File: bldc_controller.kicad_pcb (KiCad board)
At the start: 4 copper layers, 99.1 x 99.1 mm, 147 parts, among them J1 Conn_01x06_Male, J2 Banana_Jack, J3 Banana_Jack, Q1 2N7002E, Q10 IRLB8721PBF, Q11 IRLB8721PBF, Q2 DMN65D8L-7, Q3 DMN65D8L-7, Q4 MMBT3904, Q5 IRF4905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

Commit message: finished labelling
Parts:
- removed J2, J3: Banana_Jack, Connector_BarrelJack:BarrelJack_CUI_PJ-063AH_Horizontal
- added B1: Banana_Jack, Connector:CalTest_CT3151, F.Cu at (105.4, 47.0)
- added B2: CalTest_CT3151, Connector:CalTest_CT3151, F.Cu at (105.4, 61.0)
- added MH1: MountingHole_Top_Left, MountingHole:MountingHole_2.2mm_M2, F.Cu at (100.5, 38.1)
- added MH2: MountingHole_Top_Right, MountingHole:MountingHole_2.2mm_M2, F.Cu at (198.0, 38.0)
- added MH3: MountingHole_Bottom_Right, MountingHole:MountingHole_2.2mm_M2, F.Cu at (198.0, 138.5)
- added MH4: MountingHole_Bottom_Left, MountingHole:MountingHole_2.2mm_M2, F.Cu at (100.3, 138.5)
- renumbered PhaseC to PhaseA
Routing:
- net PhaseC: track 92.9 -> 106.8 mm, vias 0 -> 1
- net PhaseB: track 139.6 -> 149.8 mm
- net PhaseA: track 190.0 -> 195.5 mm
- net +BATT: track 11.9 -> 16.8 mm
- net Vdrive: track 57.9 -> 61.8 mm
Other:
- board size 99.1 x 99.1 mm -> 102.9 x 105.4 mm
- board text added: "BATT+"
- board text added: "BEMF_A"
- board text added: "BEMF_B"
- board text added: "BEMF_C"
- board text added: "Drivers"
- board text added: "EFUSE_EN"
- board text added: "I_RAW"
- board text added: "Input Connections"
- board text added: "Latching"
- board text added: "Microcontroller"
- board text added: "Neutral"
- board text added: "Overcurrent Threshold"
- board text added: "PhaseA High"
- board text added: "PhaseB High"
- board text added: "PhaseC High"
- board text added: "Power Filters"
- board text added: "Q5 Gate"
- board text added: "V Drive"
- board text added: "nI_Error"

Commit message: fixed small bug
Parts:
- moved B2 1.27 mm to (105.4, 62.2)
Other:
- board text added: "Back EMF"
- board text added: "Output to Motor"
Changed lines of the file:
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@@
   (general
     (thickness 1.6)
-    (drawings 50)
+    (drawings 54)
     (tracks 635)
     (zones 0)
@@
   (page A4)
   (layers
-    (0 F.Cu signal hide)
-    (1 In1.Cu power hide)
-    (2 In2.Cu power hide)
-    (31 B.Cu signal hide)
-    (32 B.Adhes user hide)
-    (33 F.Adhes user hide)
-    (34 B.Paste user hide)
-    (35 F.Paste user hide)
-    (36 B.SilkS user hide)
+    (0 F.Cu signal)
+    (1 In1.Cu power)
+    (2 In2.Cu power)
+    (31 B.Cu signal)
+    (32 B.Adhes user)
+    (33 F.Adhes user)
+    (34 B.Paste user)
+    (35 F.Paste user)
+    (36 B.SilkS user)
     (37 F.SilkS user)
-    (38 B.Mask user hide)
-    (39 F.Mask user hide)
-    (40 Dwgs.User user hide)
-    (41 Cmts.User user hide)
+    (38 B.Mask user)
+    (39 F.Mask user)
+    (40 Dwgs.User user)
+    (41 Cmts.User user)
     (42 Eco1.User user hide)
     (43 Eco2.User user)
     (44 Edge.Cuts user)
     (45 Margin user hide)
-    (46 B.CrtYd user hide)
-    (47 F.CrtYd user hide)
-    (48 B.Fab user hide)
-    (49 F.Fab user hide)
+    (46 B.CrtYd user)
+    (47 F.CrtYd user)
+    (48 B.Fab user)
+    (49 F.Fab user)
   )
   (setup
-    (last_trace_width 0.508)
+    (last_trace_width 0.25)
     (user_trace_width 0.254)
     (user_trace_width 0.508)
@@
     (pad_to_mask_clearance 0)
     (aux_axis_origin 0 0)
-    (visible_elements 7FFFF7FF)
+    (visible_elements 7EE6A077)
     (pcbplotparams
       (layerselection 0x010fc_ffffffff)
@@
   )
   (module Connector:CalTest_CT3151 (layer F.Cu)
-    (at 105.41 60.96)
+    (at 105.41 62.23)
     (descr "Right-angle standard banana jack, http://www.caltestelectronics.com/images/attachments/P315100rH_drawing.pdf")
     (tags "banana jack horizontal")
@@
     )
   )
+  (gr_text "Back EMF" (at 185.42 115.57) (layer F.SilkS)
+    (effects (font (size 1 1) (thickness 0.15)))
+  )
+  (gr_text "Output to Motor" (at 191.77 102.87) (layer F.SilkS)
+    (effects (font (size 1 1) (thickness 0.15)))
+  )
+  (gr_text "Output to Motor" (at 191.77 78.74) (layer F.SilkS)
+    (effects (font (size 1 1) (thickness 0.15)))
+  )
+  (gr_text "Output to Motor" (at 191.77 57.15) (layer F.SilkS)
+    (effects (font (size 1 1) (thickness 0.15)))
+  )
   (gr_text "Q5 Gate" (at 165.1 57.15) (layer F.SilkS)
     (effects (font (size 1 1) (thickness 0.15)))
@@
     (connect_pads (clearance 0.508))
     (min_thickness 0.254)
-    (fill (arc_segments 32) (thermal_gap 0.508) (thermal_bridge_width 0.508))
+    (fill yes (arc_segments 32) (thermal_gap 0.508) (thermal_bridge_width 0.508))
     (polygon
       (pts
@@
     (connect_pads (clearance 0.508))
     (min_thickness 0.254)
-    (fill (arc_segments 32) (thermal_gap 0.508) (thermal_bridge_width 0.508))
+    (fill yes (arc_segments 32) (thermal_gap 0.508) (thermal_bridge_width 0.508))
     (polygon
       (pts

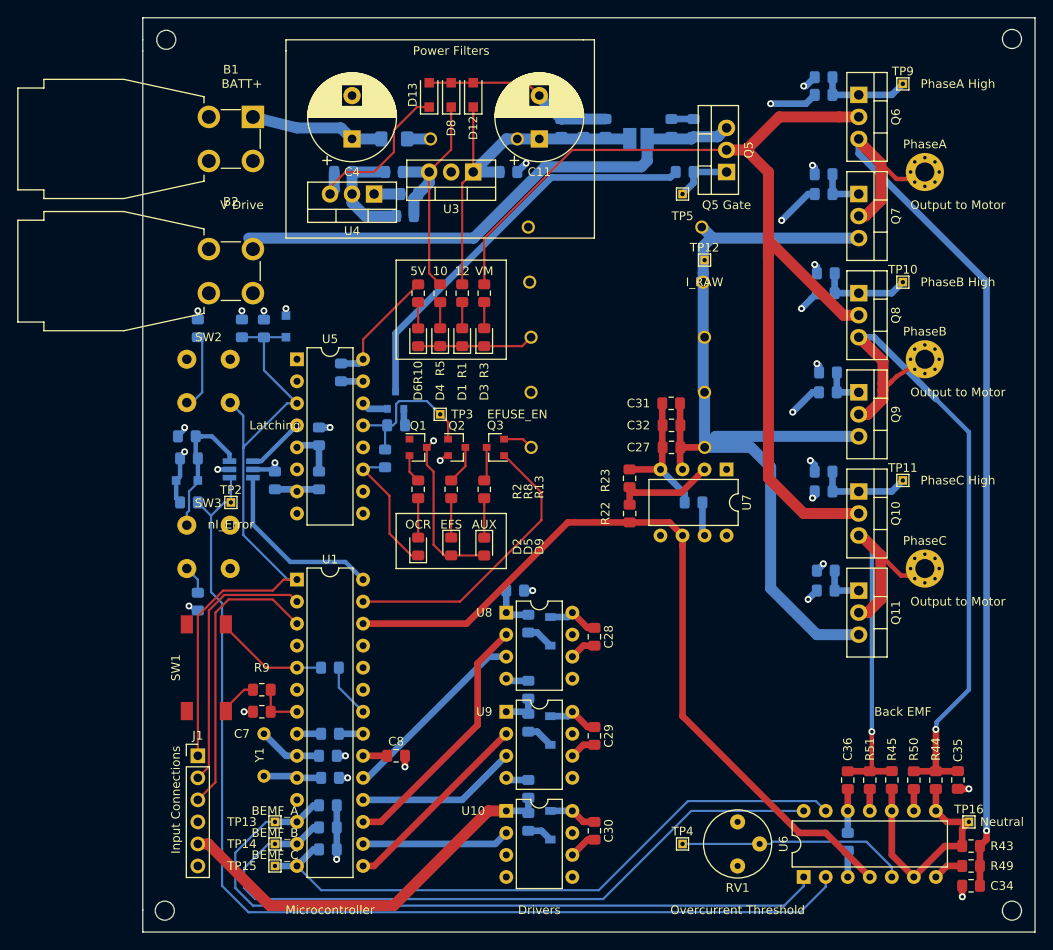
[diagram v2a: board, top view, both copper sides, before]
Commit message: fixed wire thickness
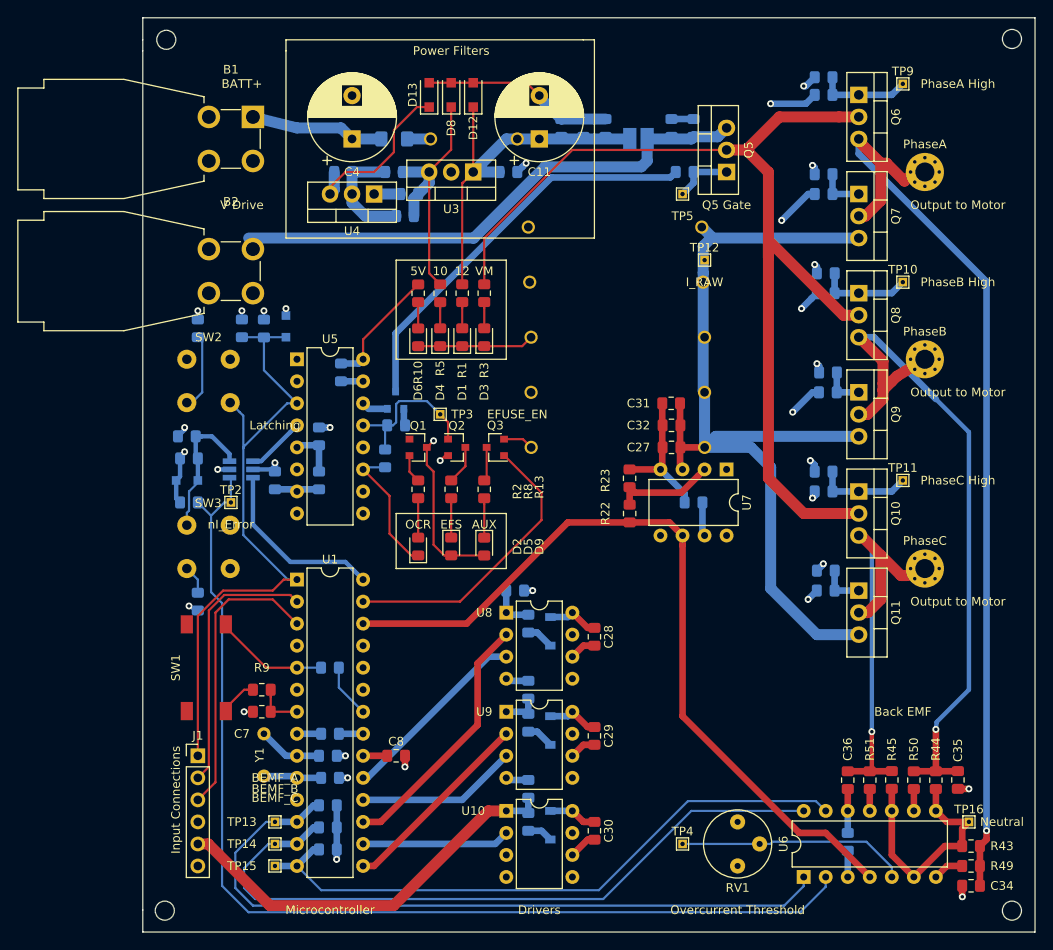
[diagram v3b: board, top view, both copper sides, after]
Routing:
- net PhaseA: track 195.5 -> 198.4 mm
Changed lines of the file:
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@@
     (thickness 1.6)
     (drawings 54)
-    (tracks 635)
+    (tracks 636)
     (zones 0)
     (modules 151)
@@
   (layers
     (0 F.Cu signal)
-    (1 In1.Cu power)
-    (2 In2.Cu power)
-    (31 B.Cu signal)
-    (32 B.Adhes user)
+    (1 In1.Cu power hide)
+    (2 In2.Cu power hide)
+    (31 B.Cu signal hide)
+    (32 B.Adhes user hide)
     (33 F.Adhes user)
-    (34 B.Paste user)
+    (34 B.Paste user hide)
     (35 F.Paste user)
-    (36 B.SilkS user)
+    (36 B.SilkS user hide)
     (37 F.SilkS user)
-    (38 B.Mask user)
+    (38 B.Mask user hide)
     (39 F.Mask user)
     (40 Dwgs.User user)
-    (41 Cmts.User user)
+    (41 Cmts.User user hide)
     (42 Eco1.User user hide)
-    (43 Eco2.User user)
+    (43 Eco2.User user hide)
     (44 Edge.Cuts user)
     (45 Margin user hide)
-    (46 B.CrtYd user)
+    (46 B.CrtYd user hide)
     (47 F.CrtYd user)
-    (48 B.Fab user)
-    (49 F.Fab user)
+    (48 B.Fab user hide)
+    (49 F.Fab user hide)
   )
   (setup
-    (last_trace_width 0.25)
+    (last_trace_width 1.27)
     (user_trace_width 0.254)
     (user_trace_width 0.508)
@@
     (mod_text_size 1 1)
     (mod_text_width 0.15)
-    (pad_size 2.2 2.2)
+    (pad_size 4.4 4.4)
     (pad_drill 2.2)
     (pad_to_mask_clearance 0)
     (aux_axis_origin 0 0)
-    (visible_elements 7EE6A077)
+    (visible_elements 7EFFA6FF)
     (pcbplotparams
       (layerselection 0x010fc_ffffffff)
@@
       (effects (font (size 1 1) (thickness 0.15)))
     )
-    (pad 1 thru_hole circle (at 1.166726 -1.166726) (size 0.7 0.7) (drill 0.4) (layers *.Cu *.Mask))
-    (pad 1 thru_hole circle (at 0 -1.65) (size 0.7 0.7) (drill 0.4) (layers *.Cu *.Mask))
-    (pad 1 thru_hole circle (at -1.166726 -1.166726) (size 0.7 0.7) (drill 0.4) (layers *.Cu *.Mask))
-    (pad 1 thru_hole circle (at -1.65 0) (size 0.7 0.7) (drill 0.4) (layers *.Cu *.Mask))
-    (pad 1 thru_hole circle (at -1.166726 1.166726) (size 0.7 0.7) (drill 0.4) (layers *.Cu *.Mask))
-    (pad 1 thru_hole circle (at 0 1.65) (size 0.7 0.7) (drill 0.4) (layers *.Cu *.Mask))
-    (pad 1 thru_hole circle (at 1.166726 1.166726) (size 0.7 0.7) (drill 0.4) (layers *.Cu *.Mask))
-    (pad 1 thru_hole circle (at 1.65 0) (size 0.7 0.7) (drill 0.4) (layers *.Cu *.Mask))
+    (pad 1 thru_hole circle (at 1.166726 -1.166726) (size 0.7 0.7) (drill 0.4) (layers *.Cu *.Mask)
+      (net 14 PhaseA))
+    (pad 1 thru_hole circle (at 0 -1.65) (size 0.7 0.7) (drill 0.4) (layers *.Cu *.Mask)
+      (net 14 PhaseA))
+    (pad 1 thru_hole circle (at -1.166726 -1.166726) (size 0.7 0.7) (drill 0.4) (layers *.Cu *.Mask)
+      (net 14 PhaseA))
+    (pad 1 thru_hole circle (at -1.65 0) (size 0.7 0.7) (drill 0.4) (layers *.Cu *.Mask)
+      (net 14 PhaseA))
+    (pad 1 thru_hole circle (at -1.166726 1.166726) (size 0.7 0.7) (drill 0.4) (layers *.Cu *.Mask)
+      (net 14 PhaseA))
+    (pad 1 thru_hole circle (at 0 1.65) (size 0.7 0.7) (drill 0.4) (layers *.Cu *.Mask)
+      (net 14 PhaseA))
+    (pad 1 thru_hole circle (at 1.166726 1.166726) (size 0.7 0.7) (drill 0.4) (layers *.Cu *.Mask)
+      (net 14 PhaseA))
+    (pad 1 thru_hole circle (at 1.65 0) (size 0.7 0.7) (drill 0.4) (layers *.Cu *.Mask)
+      (net 14 PhaseA))
     (pad 1 thru_hole circle (at 0 0) (size 4.4 4.4) (drill 2.2) (layers *.Cu *.Mask)
       (net 14 PhaseA))
@@
     (effects (font (size 1 1) (thickness 0.15)))
   )
-  (gr_text BEMF_C (at 113.03 132.08) (layer F.SilkS)
+  (gr_text BEMF_C (at 113.03 125.5) (layer F.SilkS)
     (effects (font (size 1 1) (thickness 0.15)))
   )
-  (gr_text BEMF_B (at 113.03 129.54) (layer F.SilkS)
+  (gr_text BEMF_B (at 113.03 124.46) (layer F.SilkS)
     (effects (font (size 1 1) (thickness 0.15)))
   )
-  (gr_text BEMF_A (at 113.03 127) (layer F.SilkS)
+  (gr_text BEMF_A (at 113.03 123.19) (layer F.SilkS)
     (effects (font (size 1 1) (thickness 0.15)))
   )
@@
   (segment (start 180.34 49.784) (end 182.88 52.324) (width 1.27) (layer F.Cu) (net 14))
   (segment (start 185.924079 54.144001) (end 185.989273 54.144001) (width 0.508) (layer F.Cu) (net 14))
-  (segment (start 184.700001 54.144001) (end 185.924079 54.144001) (width 0.508) (layer F.Cu) (net 14))
-  (segment (start 182.88 52.324) (end 184.700001 54.144001) (width 0.508) (layer F.Cu) (net 14))
+  (segment (start 187.96 52.324) (end 185.608273 54.392075) (width 1.27) (layer F.Cu) (net 14))
+  (segment (start 182.88 52.324) (end 183.540198 52.324) (width 1.27) (layer F.Cu) (net 14))
+  (segment (start 183.540198 52.324) (end 185.608273 54.392075) (width 1.27) (layer F.Cu) (net 14))
   (segment (start 149.08 105.9) (end 147.32 104.14) (width 0.762) (layer F.Cu) (net 15))
   (segment (start 149.86 105.9) (end 149.08 105.9) (width 0.762) (layer F.Cu) (net 15))
@@
   (segment (start 182.102 72.39) (end 189.23 79.518) (width 0.762) (layer B.Cu) (net 16))
   (segment (start 183.896 77.724) (end 183.134 77.724) (width 0.508) (layer F.Cu) (net 16))
-  (segment (start 187.96 74.93) (end 184.719273 76.900727) (width 0.508) (layer F.Cu) (net 16))
+  (segment (start 187.96 74.93) (end 184.719273 76.900727) (width 1.27) (layer F.Cu) (net 16))
   (segment (start 183.134 75.1365) (end 183.134 77.724) (width 1.27) (layer F.Cu) (net 16))
-  (segment (start 184.15 77.47) (end 183.134 78.486) (width 0.508) (layer F.Cu) (net 16))
+  (segment (start 184.15 77.47) (end 183.134 78.486) (width 1.27) (layer F.Cu) (net 16))
   (segment (start 183.134 78.486) (end 183.134 79.502) (width 1.27) (layer F.Cu) (net 16))
   (segment (start 183.134 77.724) (end 183.134 78.486) (width 1.27) (layer F.Cu) (net 16))
-  (segment (start 184.719273 76.900727) (end 184.15 77.47) (width 0.508) (layer F.Cu) (net 16))
+  (segment (start 184.719273 76.900727) (end 184.15 77.47) (width 1.27) (layer F.Cu) (net 16))
   (segment (start 184.15 77.47) (end 183.896 77.724) (width 0.508) (layer F.Cu) (net 16))
   (segment (start 189.23 117.6) (end 189.322001 116.747999) (width 0.508) (layer B.Cu) (net 16))
@@
   (segment (start 179.07 122.428) (end 184.132 122.428) (width 0.762) (layer F.Cu) (net 18))
   (segment (start 182.88 97.536) (end 182.88 102.616) (width 1.27) (layer F.Cu) (net 18))
-  (segment (start 185.924079 99.864001) (end 185.989273 99.864001) (width 0.508) (layer F.Cu) (net 18))
-  (segment (start 187.96 99.06) (end 185.924079 99.864001) (width 0.508) (layer F.Cu) (net 18))
-  (segment (start 182.88 97.536) (end 185.208001 99.864001) (width 0.508) (layer F.Cu) (net 18))
-  (segment (start 185.208001 99.864001) (end 185.924079 99.864001) (width 0.508) (layer F.Cu) (net 18))
+  (segment (start 187.96 99.06) (end 185.924079 99.864001) (width 1.27) (layer F.Cu) (net 18))
+  (segment (start 182.88 97.536) (end 185.208001 99.864001) (width 1.27) (layer F.Cu) (net 18))
   (segment (start 180.3875 95.25) (end 181.848 96.7105) (width 0.508) (layer B.Cu) (net 18))
   (segment (start 181.848 96.7105) (end 181.848 117.872) (width 0.508) (layer B.Cu) (net 18))
@@
   (segment (start 181.848 122.19) (end 181.61 122.428) (width 0.508) (layer F.Cu) (net 18))
   (segment (start 181.848 117.872) (end 181.848 122.19) (width 0.508) (layer F.Cu) (net 18))
+  (segment (start 185.208001 99.864001) (end 185.885999 99.864001) (width 1.27) (layer F.Cu) (net 18))
+  (segment (start 185.885999 99.864001) (end 185.924079 99.864001) (width 0.508) (layer F.Cu) (net 18))
   (segment (start 148.59 128.27) (end 147.32 127) (width 0.762) (layer F.Cu) (net 19))
   (segment (start 149.86 128.27) (end 148.59 128.27) (width 0.762) (layer F.Cu) (net 19))

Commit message: Manual Revert
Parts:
- removed B1: Banana_Jack, Connector:CalTest_CT3151
- removed B2: CalTest_CT3151, Connector:CalTest_CT3151
- removed MH1: MountingHole_Top_Left, MountingHole:MountingHole_2.2mm_M2
- removed MH2: MountingHole_Top_Right, MountingHole:MountingHole_2.2mm_M2
- removed MH3: MountingHole_Bottom_Right, MountingHole:MountingHole_2.2mm_M2
- removed MH4: MountingHole_Bottom_Left, MountingHole:MountingHole_2.2mm_M2
- removed PhaseA, PhaseB, PhaseC: MountingHole_2.2mm_M2_Pad_Via, MountingHole:MountingHole_2.2mm_M2_Pad_Via
- added J2: Banana_Jack, Connector_BarrelJack:BarrelJack_CUI_PJ-063AH_Horizontal, F.Cu at (114.0, 48.3)
- added J3: Banana_Jack, Connector_BarrelJack:BarrelJack_CUI_PJ-063AH_Horizontal, F.Cu at (114.0, 61.0)
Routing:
- net PhaseC: track 106.7 -> 92.9 mm, vias 1 -> 0
- net PhaseB: track 149.8 -> 139.6 mm
- net PhaseA: track 198.4 -> 190.0 mm
- net +BATT: track 16.8 -> 11.9 mm
- net Vdrive: track 61.8 -> 57.9 mm
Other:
- board size 102.9 x 105.4 mm -> 99.1 x 99.1 mm
- board text removed: "BATT+"
- board text removed: "BEMF_A"
- board text removed: "BEMF_B"
- board text removed: "BEMF_C"
- board text removed: "Back EMF"
- board text removed: "Drivers"
- board text removed: "EFUSE_EN"
- board text removed: "I_RAW"
- board text removed: "Input Connections"
- board text removed: "Latching"
- board text removed: "Microcontroller"
- board text removed: "Neutral"
- board text removed: "Output to Motor"
- board text removed: "Overcurrent Threshold"
- board text removed: "PhaseA High"
- board text removed: "PhaseB High"
- board text removed: "PhaseC High"
- board text removed: "Power Filters"
- board text removed: "Q5 Gate"
- board text removed: "V Drive"
- board text removed: "nI_Error"
